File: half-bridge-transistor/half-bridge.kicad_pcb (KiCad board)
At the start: 2 copper layers, 98.6 x 98.6 mm, 30 parts, among them J1 Screw_Terminal_01x02, J10 Conn_01x01, J11 Conn_01x01, J12 Conn_01x01, J2 Screw_Terminal_01x02, J3 Bridge1, J6 Bridge2, J7 NegBus, J8 PosBus, J9 Conn_01x01, Q1 Q_NIGBT_GCE, Q2 Q_NIGBT_GCE

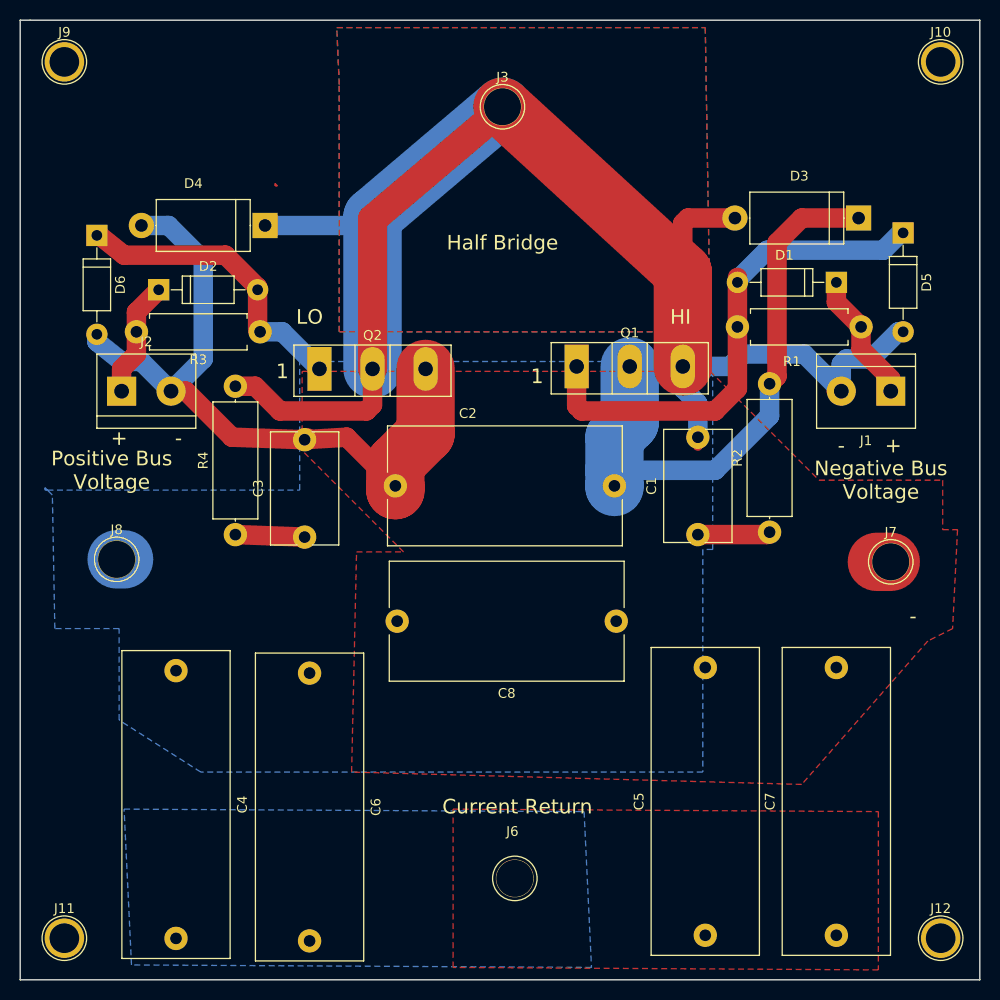
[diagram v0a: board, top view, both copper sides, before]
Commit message: Cleaned up labels and pads on half/full bridge boards
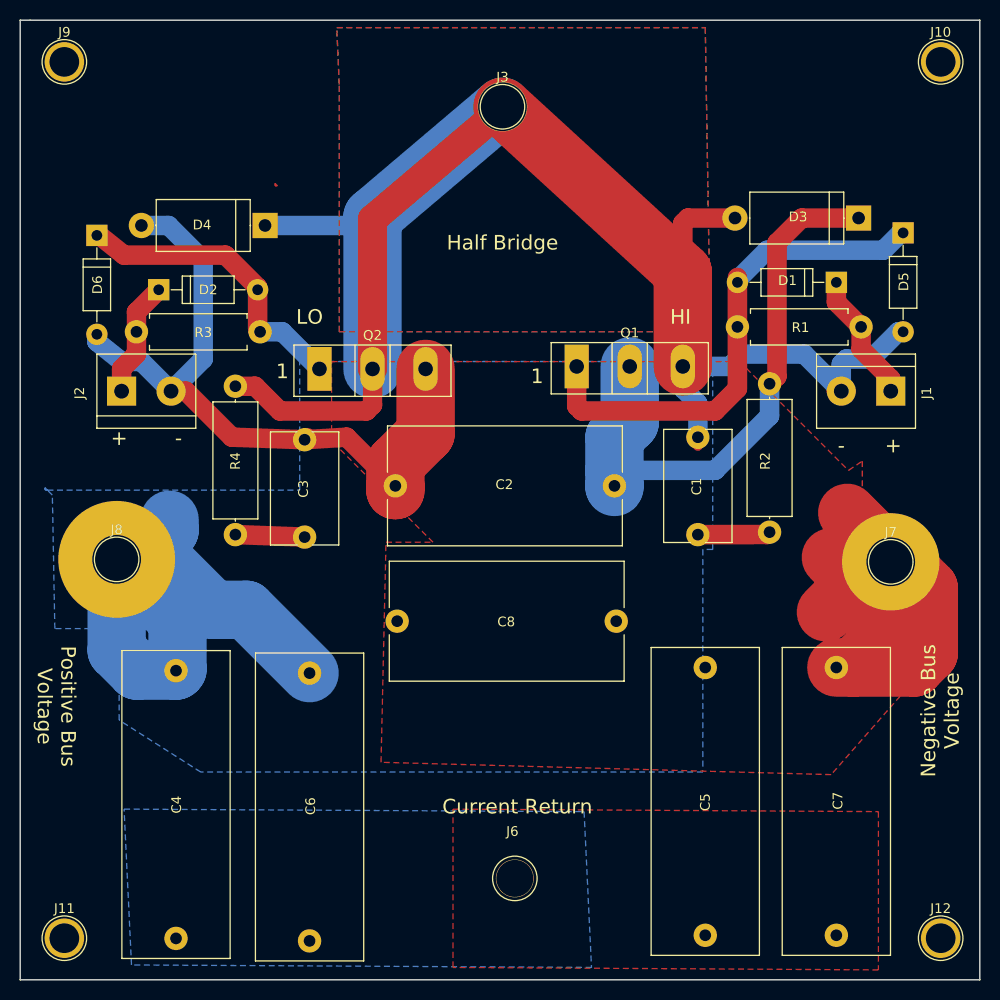
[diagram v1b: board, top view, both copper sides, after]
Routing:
- net VDD: track 59.6 -> 122.3 mm
- net GND: track 79.5 -> 135.8 mm
